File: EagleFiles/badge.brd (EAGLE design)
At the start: 50.8 x 50.8 mm, 8 parts, among them Q1 16MHz, U1 ATMEGA328P_TQFP

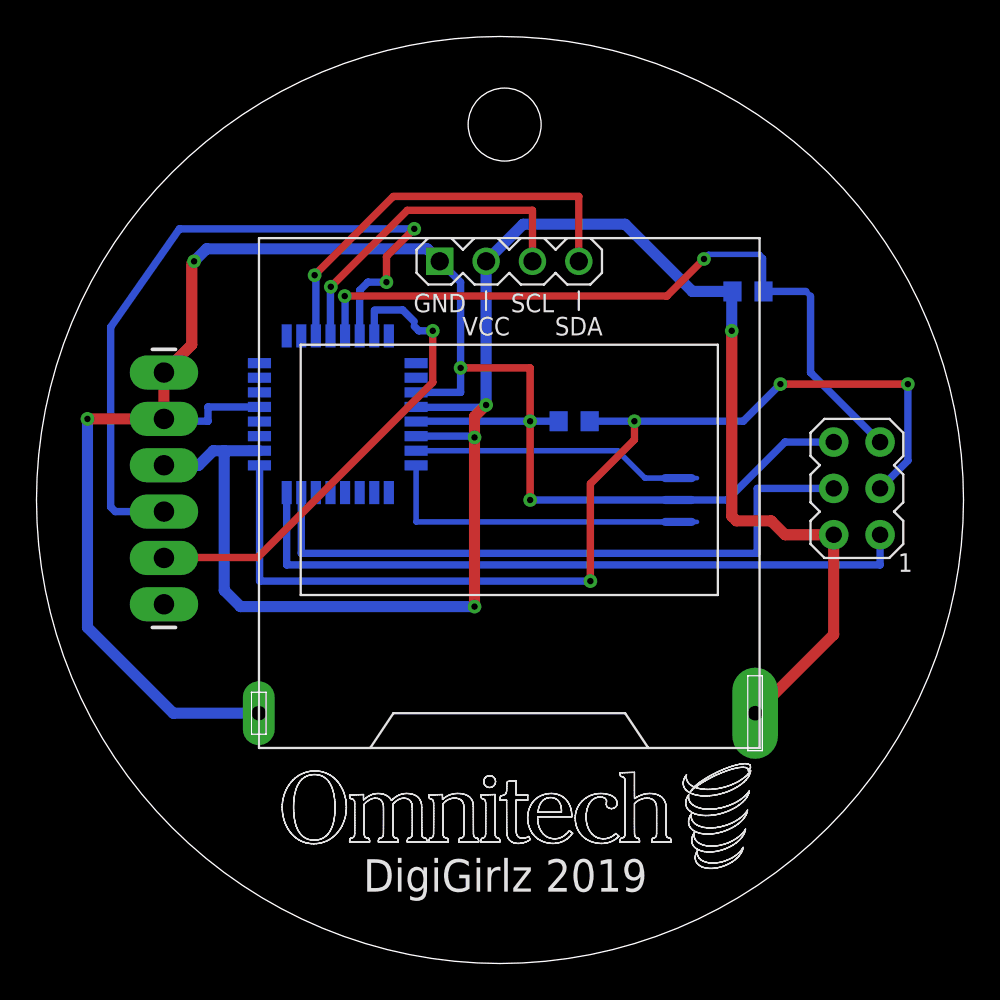
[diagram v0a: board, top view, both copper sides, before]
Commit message: Added screen documentation, updated Eagle Files, added starter Arduino sketch
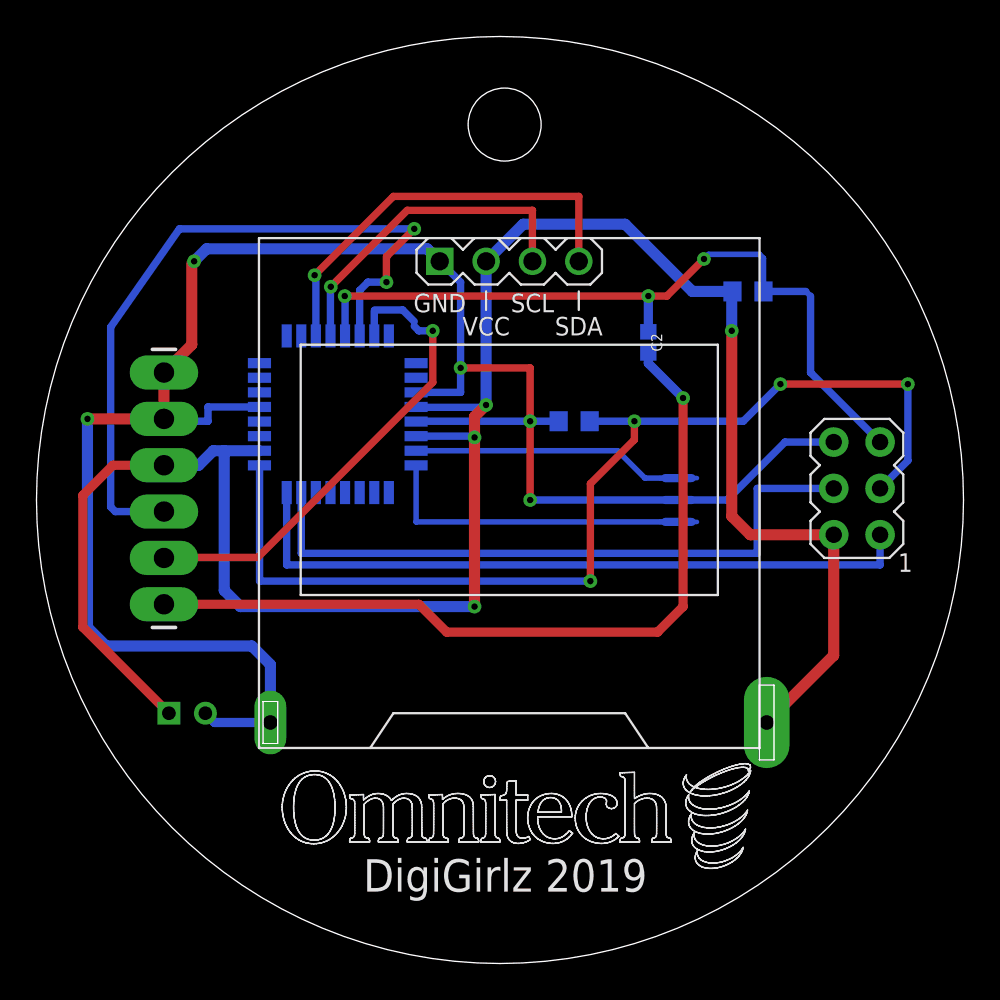
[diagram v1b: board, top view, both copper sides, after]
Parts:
- added C1: RNE1C101MDS1PX, RNE1C101MDS1PX:CAPPRD200W50D500H1000
- added C2: 0.1uF, SparkFun-Capacitors:0402
- moved BT1 0.81 mm to (26.4, 13.2)
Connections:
- net DTR: now also C2.1
- net GND: now also C1.2
- net RESET: now also C2.2
- net VCC: now also C1.1
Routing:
- net DTR: track 0.00 -> 44.3 mm, vias 0 -> 1
- net VCC: track 99.4 -> 118.7 mm
- net GND: track 103.4 -> 109.8 mm
- net RESET: track 40.3 -> 42.2 mm, vias 2 -> 3
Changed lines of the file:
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@@
 </element>
 <element name="U$1" library="diy-modules" package="DISPLAY-OLED-128X64-I2C" value="DISPLAY-OLED-128X64-I2C" x="25.908" y="25.781" smashed="yes"/>
-<element name="BT1" library="BC2032-E2" package="MPD_BC2032-E2" value="BC2032-E2" x="25.781" y="13.716" smashed="yes" rot="MR0">
-<attribute name="DESCRIPTION" value=" BATTERY HOLDER COIN 20MM PC PIN " x="25.781" y="13.716" size="1.778" layer="28" rot="MR0" display="off"/>
-<attribute name="DIGI-KEY_PART_NUMBER" value="BC2032-E2-ND" x="25.781" y="13.716" size="1.778" layer="28" rot="MR0" display="off"/>
-<attribute name="DIGI-KEY_PURCHASE_URL" value="https://www.digikey.com/product-detail/en/mpd-memory-protection-devices/BC2032-E2/BC2032-E2-ND/2077836?utm_source=snapeda&amp;utm_medium=aggregator&amp;utm_campaign=symbol" x="25.781" y="13.716" size="1.778" layer="28" rot="MR0" display="off"/>
-<attribute name="MF" value="MPD _Memory" x="25.781" y="13.716" size="1.778" layer="28" rot="MR0" display="off"/>
-<attribute name="MP" value="BC2032-E2" x="25.781" y="13.716" size="1.778" layer="28" rot="MR0" display="off"/>
-<attribute name="PACKAGE" value="None" x="25.781" y="13.716" size="1.778" layer="28" rot="MR0" display="off"/>
-<attribute name="VALUE" x="30.78863125" y="0.9465" size="1.271940625" layer="28" rot="MR0"/>
+<element name="BT1" library="BC2032-E2" package="MPD_BC2032-E2" value="BC2032-E2" x="26.416" y="13.208" smashed="yes" rot="MR0">
+<attribute name="DESCRIPTION" value=" BATTERY HOLDER COIN 20MM PC PIN " x="26.416" y="13.208" size="1.778" layer="28" rot="MR0" display="off"/>
+<attribute name="DIGI-KEY_PART_NUMBER" value="BC2032-E2-ND" x="26.416" y="13.208" size="1.778" layer="28" rot="MR0" display="off"/>
+<attribute name="DIGI-KEY_PURCHASE_URL" value="https://www.digikey.com/product-detail/en/mpd-memory-protection-devices/BC2032-E2/BC2032-E2-ND/2077836?utm_source=snapeda&amp;utm_medium=aggregator&amp;utm_campaign=symbol" x="26.416" y="13.208" size="1.778" layer="28" rot="MR0" display="off"/>
+<attribute name="MF" value="MPD _Memory" x="26.416" y="13.208" size="1.778" layer="28" rot="MR0" display="off"/>
+<attribute name="MP" value="BC2032-E2" x="26.416" y="13.208" size="1.778" layer="28" rot="MR0" display="off"/>
+<attribute name="PACKAGE" value="None" x="26.416" y="13.208" size="1.778" layer="28" rot="MR0" display="off"/>
+<attribute name="VALUE" x="31.42363125" y="0.4385" size="1.271940625" layer="28" rot="MR0"/>
+</element>
+<element name="C1" library="RNE1C101MDS1PX" package="CAPPRD200W50D500H1000" value="RNE1C101MDS1PX" x="8.255" y="13.716" smashed="yes" rot="MR180">
+<attribute name="DESCRIPTION" value=" Cap Aluminum Polymer 100uF 16VDC 20% _5 X 10mm_ Radial 2mm 0.035 Ohm 2300mA 2000h 105C T/R " x="8.255" y="13.716" size="1.778" layer="28" rot="MR180" display="off"/>
+<attribute name="DIGI-KEY_PART_NUMBER" value="493-3813-1-ND" x="8.255" y="13.716" size="1.778" layer="28" rot="MR180" display="off"/>
+<attribute name="DIGI-KEY_PURCHASE_URL" value="https://www.digikey.com/product-detail/en/nichicon/RNE1C101MDS1PX/493-3813-1-ND/2239226?utm_source=snapeda&amp;utm_medium=aggregator&amp;utm_campaign=symbol" x="8.255" y="13.716" size="1.778" layer="28" rot="MR180" display="off"/>
+<attribute name="MF" value="Nichicon" x="8.255" y="13.716" size="1.778" layer="28" rot="MR180" display="off"/>
+<attribute name="MP" value="RNE1C101MDS1PX" x="8.255" y="13.716" size="1.778" layer="28" rot="MR180" display="off"/>
+<attribute name="NAME" x="8.37831875" y="10.40848125" size="1.271840625" layer="26" rot="MR180"/>
+<attribute name="PACKAGE" value="Radial Nichicon" x="8.255" y="13.716" size="1.778" layer="28" rot="MR180" display="off"/>
+<attribute name="VALUE" x="5.70996875" y="17.533540625" size="1.272509375" layer="28" rot="MR180" align="top-left"/>
+</element>
+<element name="C2" library="SparkFun-Capacitors" library_urn="urn:adsk.eagle:library:510" package="0402" package3d_urn="urn:adsk.eagle:package:37413/1" value="0.1uF" x="33.528" y="34.036" smashed="yes" rot="MR90">
+<attribute name="NAME" x="34.29" y="34.036" size="0.6096" layer="25" font="vector" ratio="20" rot="R90" align="bottom-center"/>
+<attribute name="PROD_ID" value="CAP-12416" x="33.528" y="34.036" size="1.778" layer="28" rot="MR90" display="off"/>
+<attribute name="VALUE" x="32.766" y="34.036" size="0.6096" layer="28" font="vector" ratio="20" rot="MR90" align="top-center"/>
 </element>
 </elements>
@@
 <wire x1="42.418" y1="36.576" x2="42.164" y2="36.83" width="0.3048" layer="16"/>
 <wire x1="42.164" y1="36.83" x2="39.839" y2="36.83" width="0.4064" layer="16"/>
-<wire x1="16.891" y1="36.576" x2="34.544" y2="36.576" width="0.4064" layer="1"/>
+<wire x1="16.891" y1="36.576" x2="33.528" y2="36.576" width="0.4064" layer="1"/>
+<wire x1="33.528" y1="36.576" x2="34.544" y2="36.576" width="0.4064" layer="1"/>
 <wire x1="34.544" y1="36.576" x2="36.576" y2="38.608" width="0.4064" layer="1"/>
 <via x="36.576" y="38.608" extent="1-16" drill="0.35"/>
@@
 <wire x1="39.624" y1="38.862" x2="36.83" y2="38.862" width="0.3048" layer="16"/>
 <wire x1="36.83" y1="38.862" x2="36.576" y2="38.608" width="0.3048" layer="16"/>
+<contactref element="C2" pad="2"/>
+<via x="33.528" y="36.576" extent="1-16" drill="0.35"/>
+<wire x1="33.528" y1="34.616" x2="33.528" y2="36.576" width="0.508" layer="16"/>
 </signal>
 <signal name="SCK">
@@
 <wire x1="23.241" y1="32.639" x2="27.051" y2="32.639" width="0.4064" layer="1"/>
 <wire x1="27.051" y1="32.639" x2="27.051" y2="29.718" width="0.4064" layer="1"/>
-<wire x1="7.493" y1="13.716" x2="12.181" y2="13.716" width="0.6096" layer="16"/>
-<wire x1="2.794" y1="18.415" x2="7.493" y2="13.716" width="0.6096" layer="16"/>
+<wire x1="12.816" y1="16.383" x2="12.816" y2="13.208" width="0.6096" layer="16"/>
+<wire x1="12.816" y1="16.383" x2="11.8" y2="17.399" width="0.6096" layer="16"/>
+<wire x1="11.8" y1="17.399" x2="3.81" y2="17.399" width="0.6096" layer="16"/>
+<wire x1="2.794" y1="18.415" x2="3.81" y2="17.399" width="0.6096" layer="16"/>
+<contactref element="C1" pad="2"/>
+<wire x1="12.816" y1="13.208" x2="9.763" y2="13.208" width="0.508" layer="16"/>
+<wire x1="9.763" y1="13.208" x2="9.255" y2="13.716" width="0.508" layer="16"/>
 </signal>
 <signal name="VCC">
@@
 <wire x1="24.511" y1="30.48" x2="20.8216" y2="30.48" width="0.4064" layer="16"/>
 <wire x1="20.8216" y1="30.48" x2="20.8026" y2="30.499" width="0.3048" layer="16"/>
-<wire x1="43.688" y1="23.495" x2="41.021" y2="23.495" width="0.6096" layer="1"/>
-<wire x1="40.259" y1="24.257" x2="38.354" y2="24.257" width="0.6096" layer="1"/>
-<wire x1="41.021" y1="23.495" x2="40.259" y2="24.257" width="0.6096" layer="1"/>
-<wire x1="38.354" y1="24.257" x2="38.1" y2="24.511" width="0.6096" layer="1"/>
+<wire x1="43.688" y1="23.495" x2="39.116" y2="23.495" width="0.6096" layer="1"/>
+<wire x1="39.116" y1="23.495" x2="38.1" y2="24.511" width="0.6096" layer="1"/>
 <wire x1="38.1" y1="24.511" x2="38.1" y2="34.671" width="0.6096" layer="1"/>
 <via x="38.1" y="34.671" extent="1-16" drill="0.35"/>
@@
 <wire x1="20.8026" y1="28.899" x2="24.003" y2="28.899" width="0.4064" layer="16"/>
 <wire x1="24.003" y1="28.899" x2="24.003" y2="28.829" width="0.3048" layer="16"/>
-<wire x1="39.381" y1="13.716" x2="43.688" y2="18.023" width="0.6096" layer="1"/>
-<wire x1="43.688" y1="18.023" x2="43.688" y2="23.495" width="0.6096" layer="1"/>
+<wire x1="40.016" y1="13.208" x2="43.688" y2="16.88" width="0.6096" layer="1"/>
+<wire x1="43.688" y1="16.88" x2="43.688" y2="23.495" width="0.6096" layer="1"/>
+<contactref element="C1" pad="1"/>
+<wire x1="7.255" y1="13.716" x2="2.54" y2="18.431" width="0.508" layer="1"/>
+<wire x1="4.191" y1="27.305" x2="6.985" y2="27.305" width="0.508" layer="1"/>
+<wire x1="2.54" y1="18.431" x2="2.54" y2="25.654" width="0.508" layer="1"/>
+<wire x1="2.54" y1="25.654" x2="4.191" y2="27.305" width="0.508" layer="1"/>
 </signal>
 <signal name="XTAL1">
@@
 <signal name="DTR">
 <contactref element="J1" pad="1"/>
+<contactref element="C2" pad="1"/>
+<wire x1="6.985" y1="19.685" x2="20.955" y2="19.685" width="0.508" layer="1"/>
+<wire x1="20.955" y1="19.685" x2="22.479" y2="18.161" width="0.508" layer="1"/>
+<wire x1="22.479" y1="18.161" x2="34.036" y2="18.161" width="0.508" layer="1"/>
+<wire x1="35.433" y1="19.558" x2="35.433" y2="30.988" width="0.508" layer="1"/>
+<wire x1="34.036" y1="18.161" x2="35.433" y2="19.558" width="0.508" layer="1"/>
+<via x="35.433" y="30.988" extent="1-16" drill="0.35"/>
+<wire x1="35.433" y1="30.988" x2="33.528" y2="32.893" width="0.508" layer="16"/>
+<wire x1="33.528" y1="32.893" x2="33.528" y2="33.456" width="0.508" layer="16"/>
 </signal>
 <signal name="RX">
